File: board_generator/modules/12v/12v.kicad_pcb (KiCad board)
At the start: 2 copper layers, 22.9 x 20.3 mm, 5 parts, among them J1 Screw_Terminal_01x01, J2 Screw_Terminal_01x01, X1 interface, X2 interface

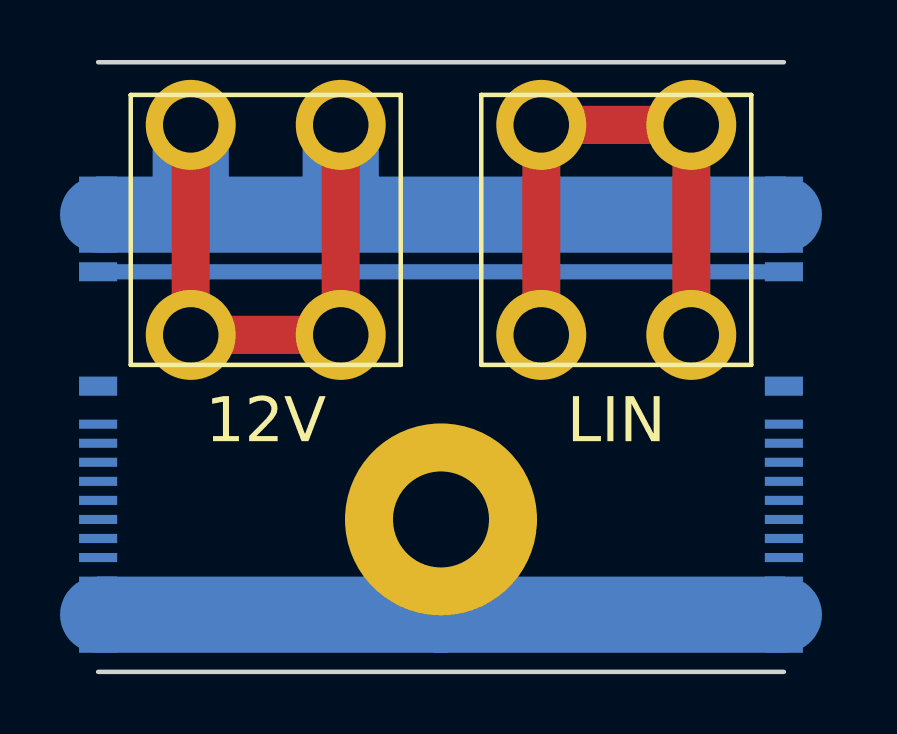
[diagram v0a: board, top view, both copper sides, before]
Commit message: Using solder pads for 12v module
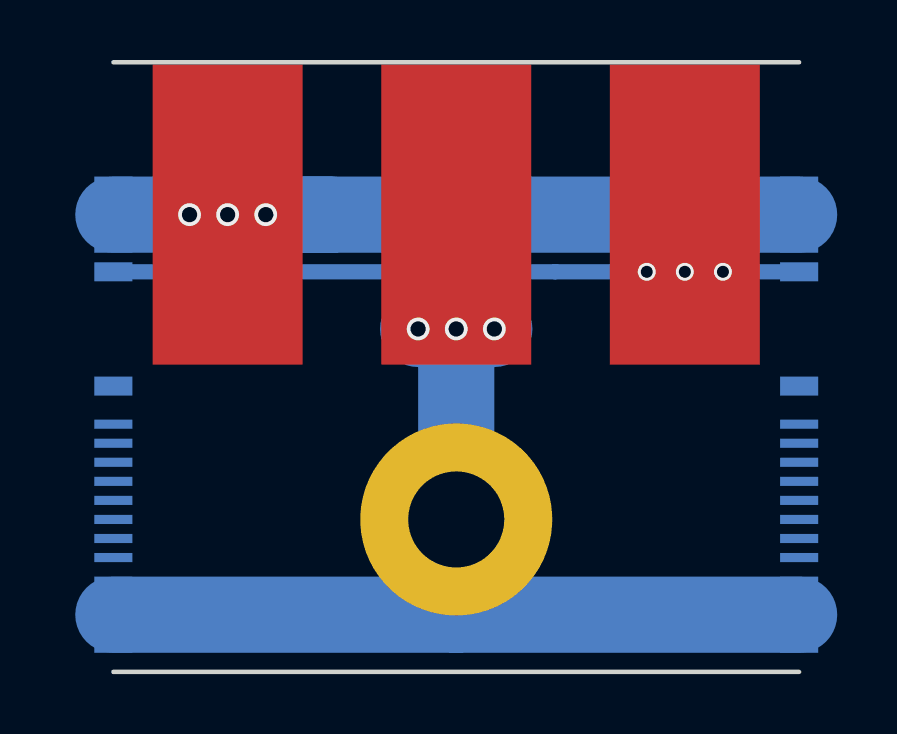
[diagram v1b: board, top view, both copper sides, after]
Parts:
- added J3: Conn_01x01, Wire_Pads:SolderWirePad_single_SMD_5x10mm, F.Cu at (139.7, 109.2)
- J1, J2: value Screw_Terminal_01x01 -> Conn_01x01; footprint connectors:TERM_SCREW_M3 -> Wire_Pads:SolderWirePad_single_SMD_5x10mm
- moved J2 2.34 mm to (147.3, 109.2)
- moved J1 1.37 mm to (132.1, 109.2)
- moved X1 0.51 mm to (128.3, 104.8)
- moved MK1 0.51 mm to (139.7, 119.4)
- moved X2 0.51 mm to (151.1, 104.8)
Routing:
- net Net-(J2-Pad1): track 46.1 -> 22.9 mm, vias 0 -> 3
- net Net-(J1-Pad1): track 48.0 -> 26.8 mm, vias 0 -> 3
- net Net-(J3-Pad1): track 26.0 -> 34.9 mm, vias 0 -> 3
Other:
- board text added: "GND"
